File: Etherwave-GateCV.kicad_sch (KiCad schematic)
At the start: 80 parts, among them J1 Etherwave Brd, J2 Volume CV, J3 Pitch CV, J4 Gate, Q1 PMP4501Y, Q2 PMBT3906, Q3 PMP4501Y, U1 LM13700, U2 CD4093, U3 CD4093, U4 CD4022, U5 TL072, U6 CD4016, U7 TL072

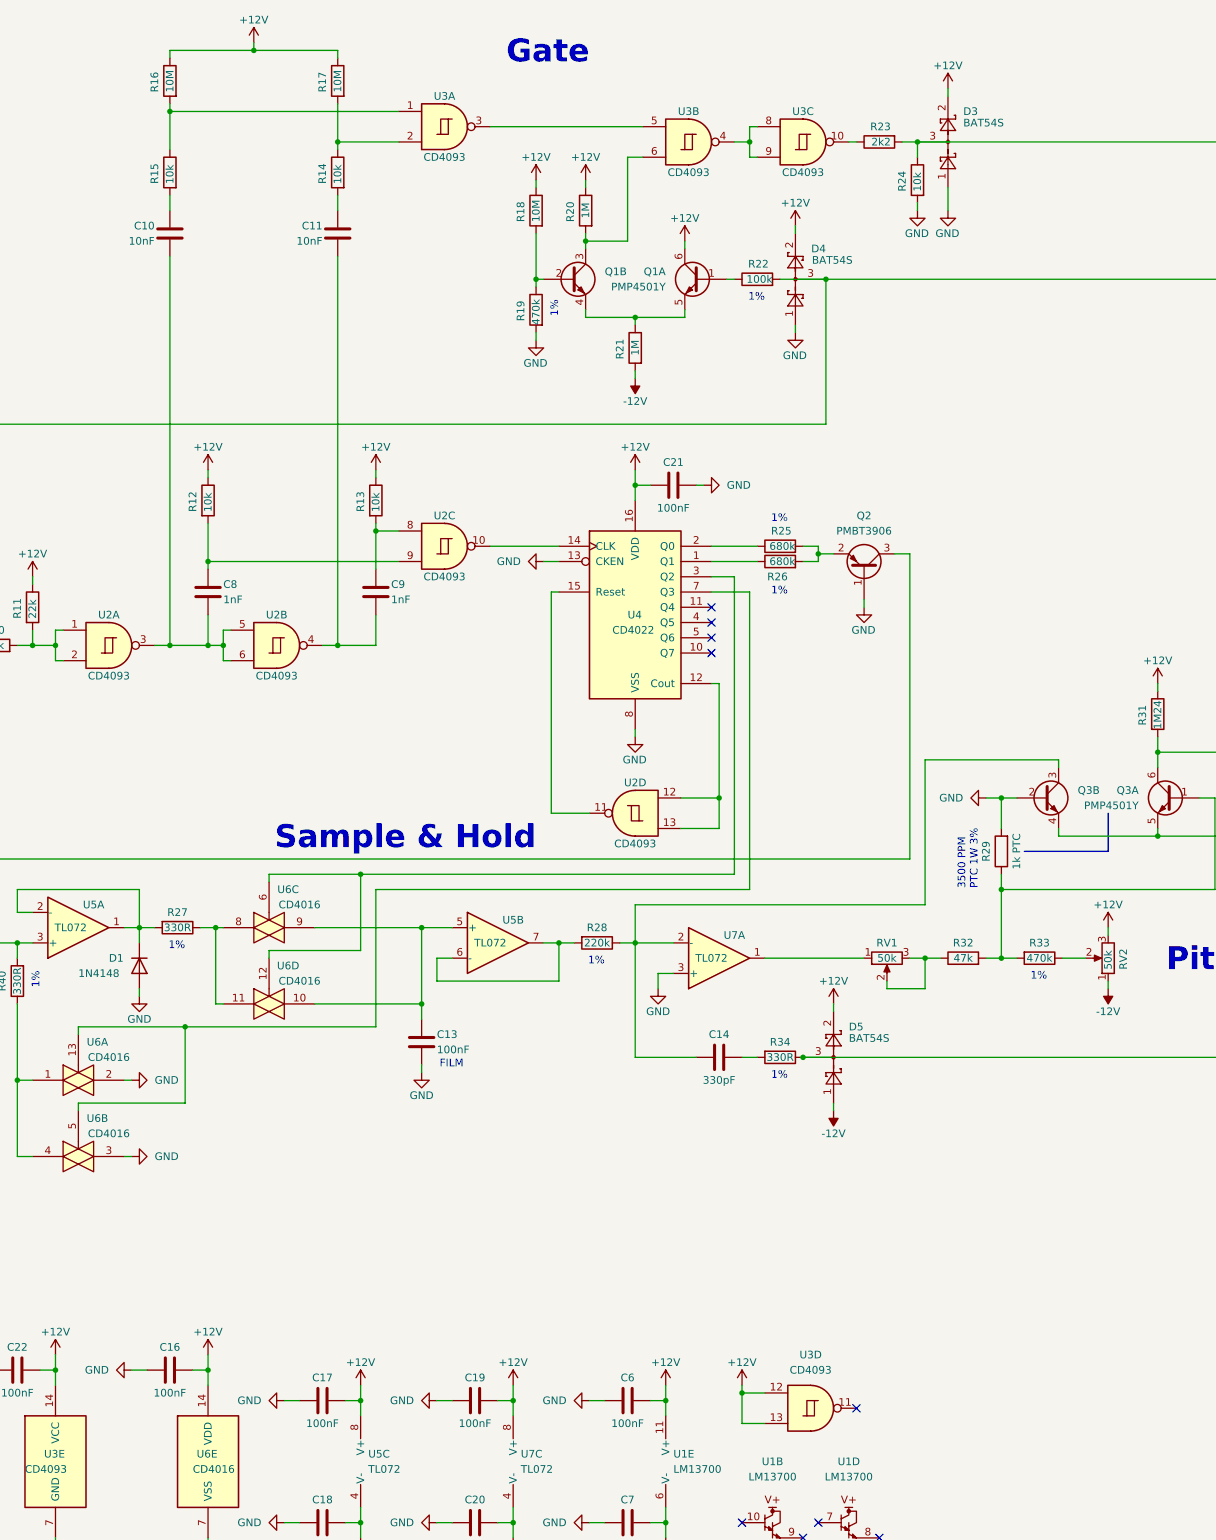
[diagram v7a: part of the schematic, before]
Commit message: added missing connection U7-A-1, C14, P1-1, R14. replaces hotfix
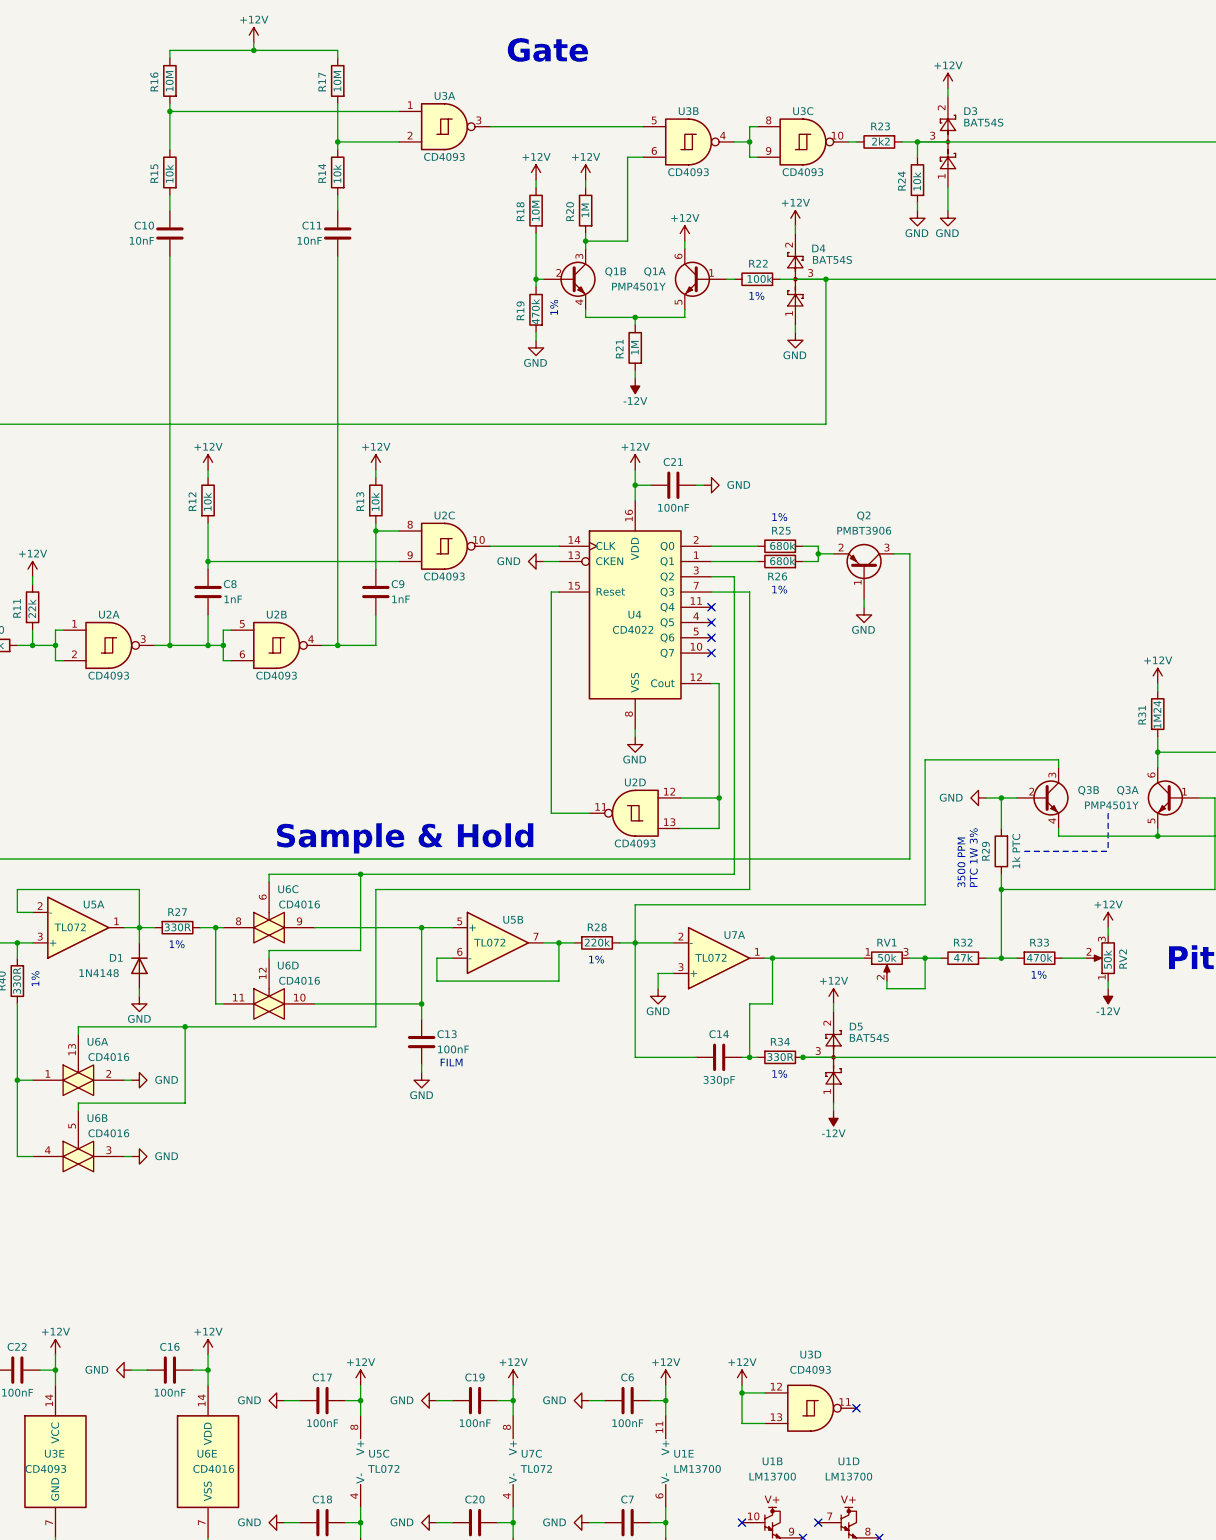
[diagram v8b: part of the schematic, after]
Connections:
- net at RV1.1, U7.1: now also C14.2, R34.2
